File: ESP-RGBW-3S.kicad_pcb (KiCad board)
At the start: 2 copper layers, 66.7 x 48.3 mm, 47 parts, among them J1 12V IN, J2 PROG, J3 LED Str., J4 Temp. S., J5 Light. S., J6 PIR, Q1 IRLML0040TRPBF, Q2 IRLML0040TRPBF, Q3 IRLML0040TRPBF, Q4 IRLML0040TRPBF, SW1 Flash, U2 ESP-12E, U4 DCDC_LM2596

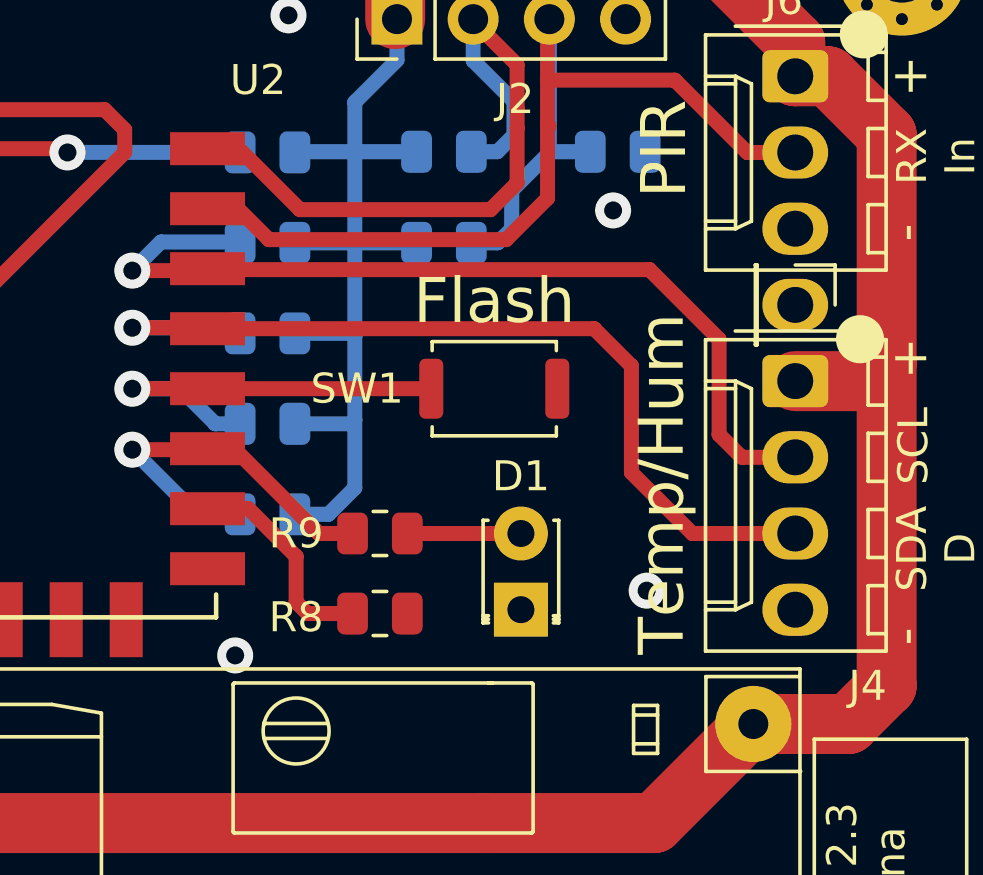
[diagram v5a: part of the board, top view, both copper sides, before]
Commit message: oprional pull-down resistors for GPIO 4-5
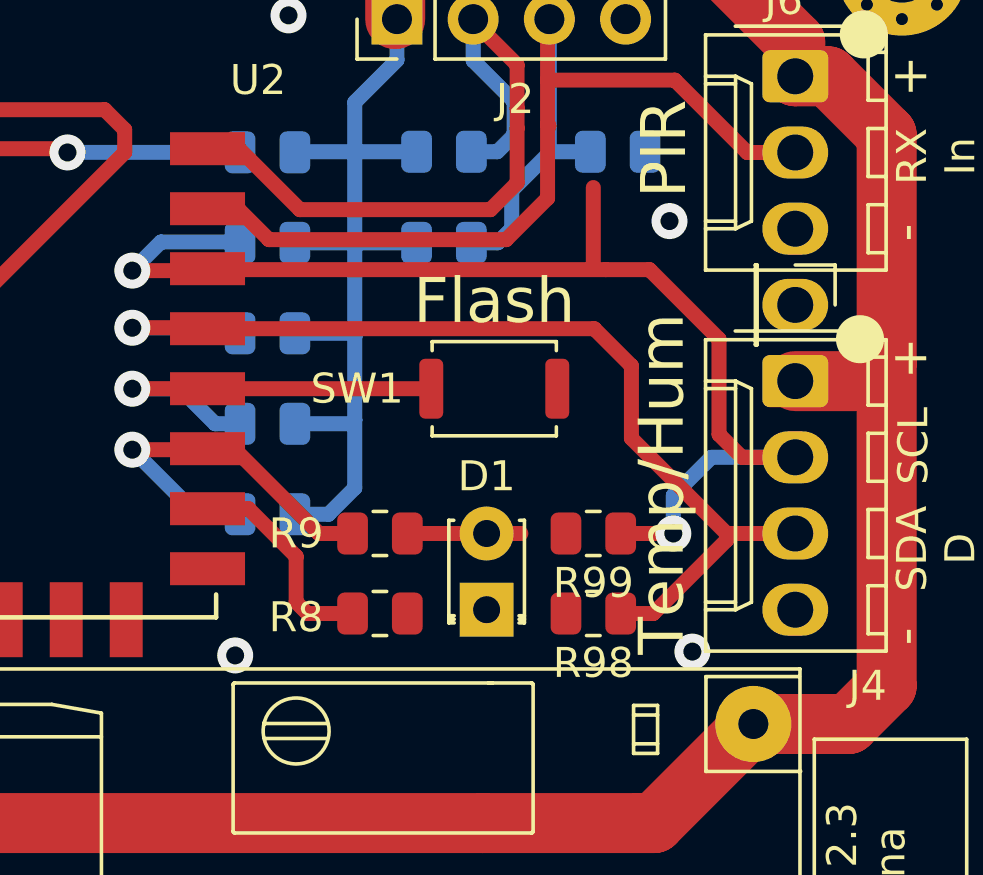
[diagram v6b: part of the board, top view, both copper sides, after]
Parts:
- added R98: 10K, Resistor_SMD:R_0805_2012Metric, F.Cu at (72.6, 49.7)
- added R99: 10K, Resistor_SMD:R_0805_2012Metric, F.Cu at (72.6, 47.0)
- moved D1 1.14 mm to (69.1, 49.5)
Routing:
- net /SCL: track 31.2 -> 41.5 mm, vias 1 -> 2
- net /SDA-DATA: track 30.8 -> 34.9 mm

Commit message: Update ESP-RGBW-3S.kicad_pcb
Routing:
- net /SCL: track 41.5 -> 38.5 mm
- net GND: vias 5 -> 4
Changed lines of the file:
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@@
     (thickness 1.6)
     (drawings 49)
-    (tracks 287)
+    (tracks 285)
     (zones 0)
     (modules 49)
@@
     (tags resistor)
     (attr smd)
-    (fp_text reference R99 (at 0 -1.65) (layer F.SilkS)
+    (fp_text reference R99 (at -0.127 1.524) (layer F.SilkS)
       (effects (font (size 1 1) (thickness 0.15)))
     )
@@
     (tags resistor)
     (attr smd)
-    (fp_text reference R9 (at -2.794 0) (layer F.SilkS)
+    (fp_text reference R9 (at 0 -1.524) (layer F.SilkS)
       (effects (font (size 1 1) (thickness 0.15)))
     )
@@
     (tags resistor)
     (attr smd)
-    (fp_text reference R8 (at -2.794 0.127) (layer F.SilkS)
+    (fp_text reference R8 (at 0 1.651) (layer F.SilkS)
       (effects (font (size 1 1) (thickness 0.15)))
     )
@@
   (gr_line (start 19.05 73.025) (end 19.05 25.4) (layer Edge.Cuts) (width 0.05))
   (via (at 75.311 46.99) (size 1.2) (drill 0.6) (layers F.Cu B.Cu) (net 12))
-  (via (at 75.946 50.927) (size 1.2) (drill 0.6) (layers F.Cu B.Cu) (net 1))
   (via (at 75.184 36.576) (size 1.2) (drill 0.6) (layers F.Cu B.Cu) (net 1))
   (via (at 33.274 50.546) (size 1.2) (drill 0.6) (layers F.Cu B.Cu) (net 1))
@@
   (segment (start 60.84125 37.27196) (end 60.87046 37.30117) (width 0.5) (layer B.Cu) (net 12))
   (segment (start 58.23204 37.27196) (end 60.84125 37.27196) (width 0.5) (layer B.Cu) (net 12))
-  (segment (start 77.597 44.45) (end 79.375 44.45) (width 0.5) (layer F.Cu) (net 12))
-  (segment (start 76.835 40.513) (end 76.835 43.688) (width 0.5) (layer F.Cu) (net 12))
-  (segment (start 74.517022 38.195022) (end 76.835 40.513) (width 0.5) (layer F.Cu) (net 12))
-  (segment (start 76.835 43.688) (end 77.597 44.45) (width 0.5) (layer F.Cu) (net 12))
-  (segment (start 59.085 38.163) (end 59.117022 38.195022) (width 0.5) (layer F.Cu) (net 12))
-  (segment (start 72.644 35.4565) (end 72.644 38.1) (width 0.5) (layer F.Cu) (net 12))
-  (segment (start 73.056978 38.195022) (end 74.517022 38.195022) (width 0.5) (layer F.Cu) (net 12))
-  (segment (start 59.117022 38.195022) (end 73.056978 38.195022) (width 0.5) (layer F.Cu) (net 12))
   (segment (start 73.5565 46.99) (end 75.311 46.99) (width 0.5) (layer F.Cu) (net 12))
   (segment (start 76.581 44.45) (end 79.375 44.45) (width 0.5) (layer B.Cu) (net 12))
   (segment (start 75.311 45.72) (end 76.581 44.45) (width 0.5) (layer B.Cu) (net 12))
   (segment (start 75.311 46.99) (end 75.311 45.72) (width 0.5) (layer B.Cu) (net 12))
+  (segment (start 78.105 44.45) (end 79.375 44.45) (width 0.5) (layer F.Cu) (net 12))
+  (segment (start 76.835 43.18) (end 78.105 44.45) (width 0.5) (layer F.Cu) (net 12))
+  (segment (start 59.117022 38.195022) (end 74.517022 38.195022) (width 0.5) (layer F.Cu) (net 12))
+  (segment (start 76.835 40.513) (end 76.835 43.18) (width 0.5) (layer F.Cu) (net 12))
+  (segment (start 74.517022 38.195022) (end 76.835 40.513) (width 0.5) (layer F.Cu) (net 12))
+  (segment (start 59.085 38.163) (end 59.117022 38.195022) (width 0.5) (layer F.Cu) (net 12))
   (via (at 57.277 40.132) (size 1.2) (drill 0.6) (layers F.Cu B.Cu) (net 13))
   (segment (start 57.15 40.132) (end 57.277 40.132) (width 0.5) (layer B.Cu) (net 13))
@@
   (segment (start 57.277 40.132) (end 60.68504 40.132) (width 0.5) (layer B.Cu) (net 13))
   (segment (start 77.089 46.99) (end 79.375 46.99) (width 0.5) (layer F.Cu) (net 13))
-  (segment (start 73.914 43.815) (end 77.089 46.99) (width 0.5) (layer F.Cu) (net 13))
-  (segment (start 73.914 41.402) (end 73.914 43.815) (width 0.5) (layer F.Cu) (net 13))
+  (segment (start 77.089 47.879) (end 77.089 46.99) (width 0.5) (layer F.Cu) (net 13))
+  (segment (start 75.311 49.657) (end 77.089 47.879) (width 0.5) (layer F.Cu) (net 13))
+  (segment (start 73.5565 49.657) (end 75.311 49.657) (width 0.5) (layer F.Cu) (net 13))
+  (segment (start 77.089 46.228) (end 77.089 46.99) (width 0.5) (layer F.Cu) (net 13))
+  (segment (start 73.914 43.053) (end 77.089 46.228) (width 0.5) (layer F.Cu) (net 13))
+  (segment (start 73.914 41.402) (end 73.914 43.053) (width 0.5) (layer F.Cu) (net 13))
   (segment (start 72.675 40.163) (end 73.914 41.402) (width 0.5) (layer F.Cu) (net 13))
   (segment (start 59.085 40.163) (end 72.675 40.163) (width 0.5) (layer F.Cu) (net 13))
-  (segment (start 77.089 47.210002) (end 77.089 46.99) (width 0.5) (layer F.Cu) (net 13))
-  (segment (start 74.642002 49.657) (end 77.089 47.210002) (width 0.5) (layer F.Cu) (net 13))
-  (segment (start 73.5565 49.657) (end 74.642002 49.657) (width 0.5) (layer F.Cu) (net 13))
   (segment (start 31.099 27.271) (end 37.558 27.271) (width 0.5) (layer B.Cu) (net 14))
   (segment (start 38.162 27.875) (end 38.162 29.021) (width 0.5) (layer B.Cu) (net 14))

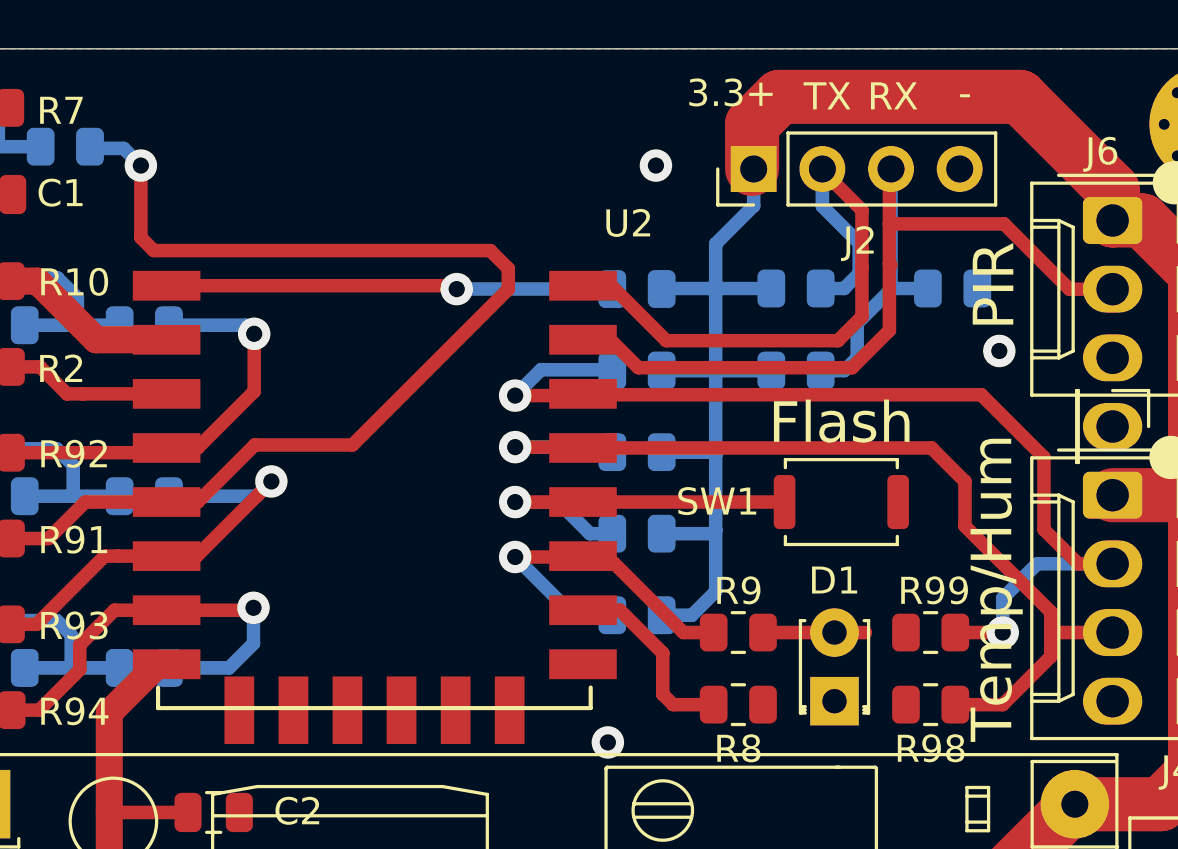
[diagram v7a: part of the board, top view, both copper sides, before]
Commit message: bottom resistors realigment
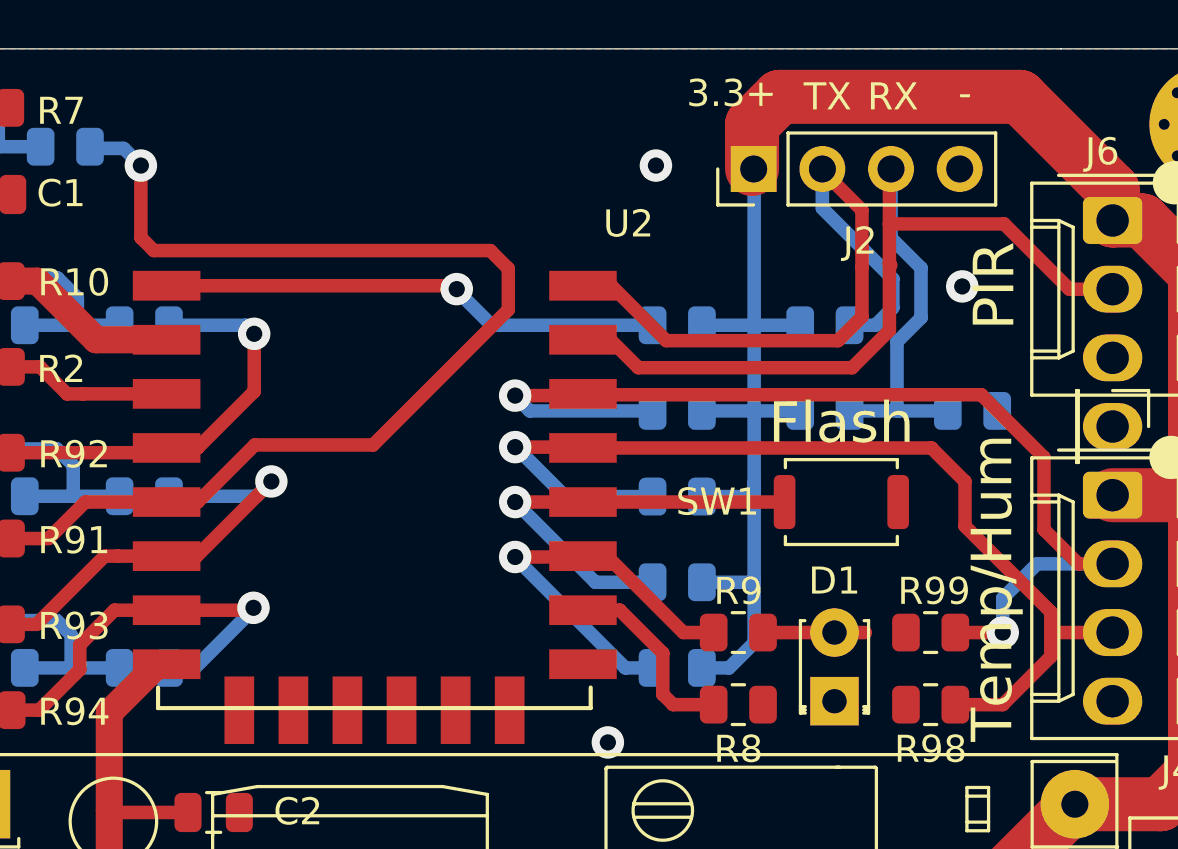
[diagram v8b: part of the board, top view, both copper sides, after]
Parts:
- moved R97 4.59 mm to (74.2, 38.8)
- moved R3 2.45 mm to (63.3, 48.3)
- moved R4 2.33 mm to (63.3, 45.1)
- moved R5 2.22 mm to (63.3, 42.0)
- moved R6 2.11 mm to (63.3, 38.8)
- moved R1 2.00 mm to (63.3, 35.6)
- moved R96 1.83 mm to (68.7, 38.8)
- moved R95 1.73 mm to (68.7, 35.6)
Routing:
- net RXD: track 38.8 -> 41.8 mm
- net /LED: track 12.9 -> 15.2 mm
- net Net-(R4-Pad2): track 14.0 -> 16.3 mm
- net /SDA-DATA: track 35.3 -> 37.5 mm
- net Net-(R1-Pad2): track 16.0 -> 18.1 mm
- net TXD: track 24.4 -> 26.4 mm
- net /SCL: track 38.5 -> 39.9 mm
- net +3V3: track 190.7 -> 191.5 mm
- net White: track 15.9 -> 15.1 mm
